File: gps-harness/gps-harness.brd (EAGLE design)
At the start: 36.3 x 40.7 mm, 7 parts

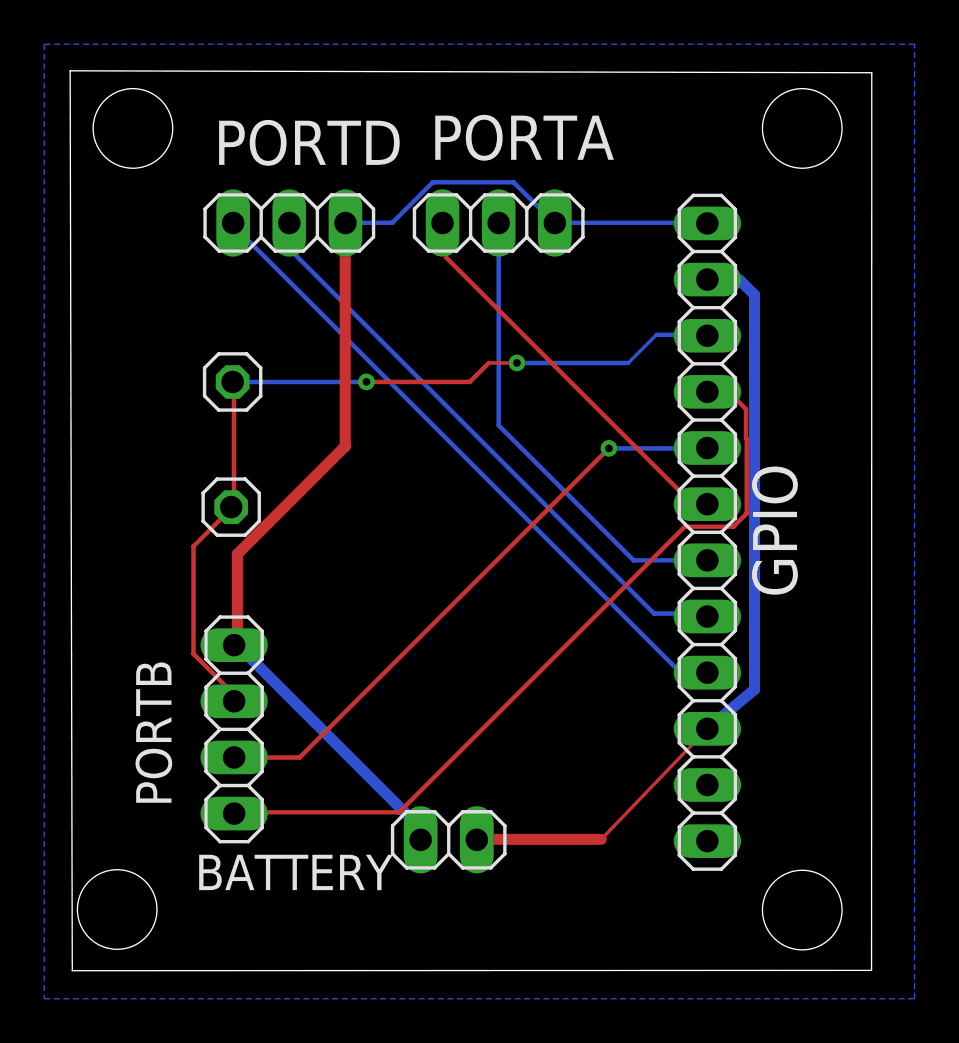
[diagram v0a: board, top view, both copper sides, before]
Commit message: Modify the place of the left bottom mounting hole; Unify the width of the wires; clear up the GND line since there's a ground plane
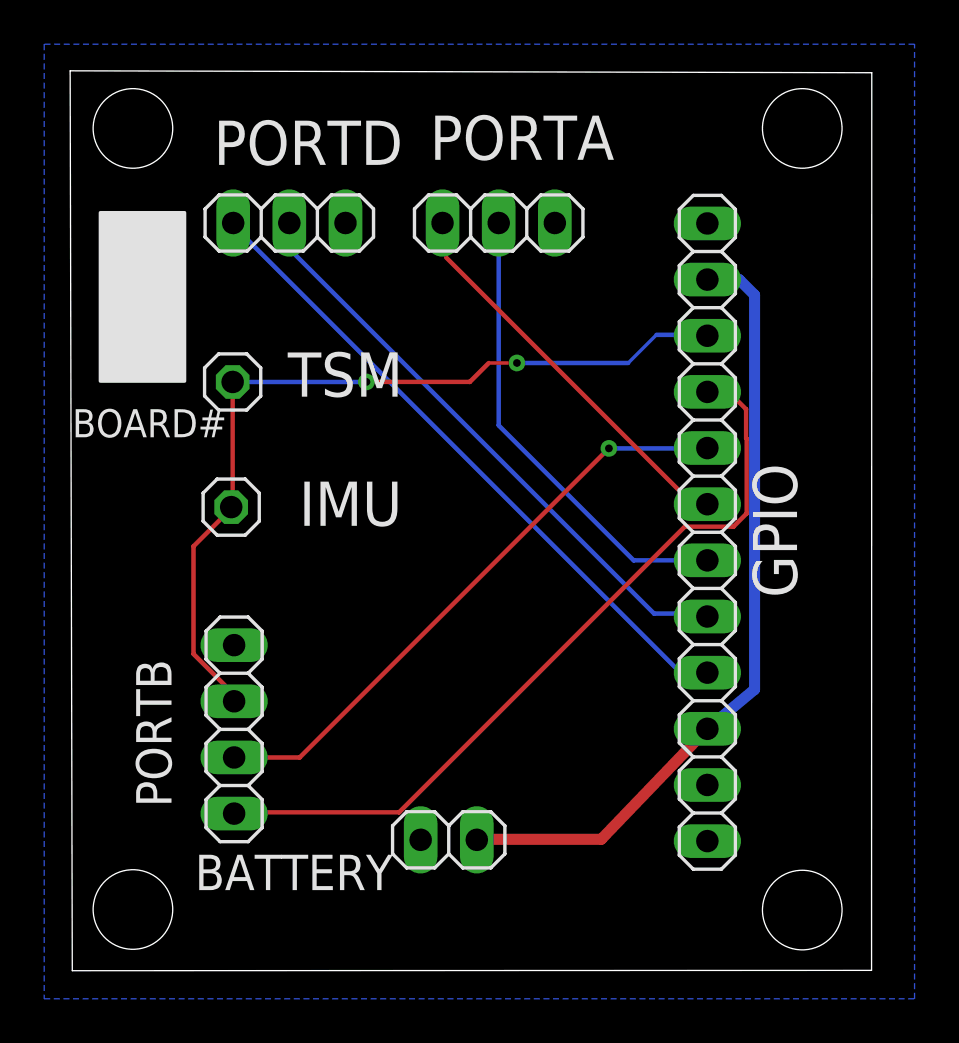
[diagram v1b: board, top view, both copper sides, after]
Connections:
- removed net NO_CONNECTION: GPIO.11, GPIO.12
- new net NC_1: GPIO.11
- new net NC_2: GPIO.12
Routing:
- net GND: track 52.0 -> 0.58 mm
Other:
- board text added: "BOARD#"
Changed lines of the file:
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@@
 <hole x="2.7432" y="38.1" drill="3.6" locked="yes"/>
 <hole x="33.02" y="2.7432" drill="3.6" locked="yes"/>
-<text x="10.256521875" y="20.124421875" size="2" layer="22">IMU</text>
-<text x="9.751059375" y="25.966421875" size="2" layer="22">TSM</text>
-<hole x="2.032" y="2.7686" drill="3.6" locked="yes"/>
+<text x="10.256521875" y="20.124421875" size="2" layer="21">IMU</text>
+<text x="9.751059375" y="25.966421875" size="2" layer="21">TSM</text>
+<hole x="2.7432" y="2.7686" drill="3.6"/>
 <hole x="33.02" y="38.1" drill="3.6" locked="yes"/>
 <text x="26.512515625" y="2.031996875" locked="yes" size="2" layer="22" rot="MR0">Autorally
@@
 v1.0
 Oct. 2019</text>
+<polygon width="0.1524" layer="21">
+<vertex x="1.27" y="34.29"/>
+<vertex x="1.27" y="26.67"/>
+<vertex x="5.08" y="26.67"/>
+<vertex x="5.08" y="34.29"/>
+</polygon>
+<text x="0" y="24.13" size="1.27" layer="21">BOARD#</text>
 </plain>
 <attributes>
@@
 <contactref element="BATTERY" pad="2"/>
 <wire x1="7.320278125" y1="14.726921875" x2="7.472675" y2="14.726921875" width="0.5" layer="16"/>
-<wire x1="16.17471875" y1="6.024878125" x2="7.472675" y2="14.726921875" width="0.5" layer="16"/>
-<wire x1="16.17471875" y1="6.024878125" x2="15.758159375" y2="5.920740625" width="0.1524" layer="16"/>
-<wire x1="14.478" y1="33.8328" x2="12.4968" y2="33.8328" width="0.2032" layer="16"/>
-<wire x1="16.3068" y1="35.6616" x2="14.478" y2="33.8328" width="0.2032" layer="16"/>
-<wire x1="19.9644" y1="35.6616" x2="16.3068" y2="35.6616" width="0.2032" layer="16"/>
-<wire x1="21.7932" y1="33.8328" x2="19.9644" y2="35.6616" width="0.2032" layer="16"/>
 <wire x1="12.4968" y1="33.8328" x2="12.3571" y2="33.822640625" width="0.1524" layer="16"/>
 <wire x1="21.7932" y1="33.8328" x2="21.8287625" y2="33.8226375" width="0.1524" layer="16"/>
-<wire x1="21.9456" y1="33.8328" x2="28.6004" y2="33.8328" width="0.2032" layer="16"/>
 <wire x1="28.6004" y1="33.8328" x2="28.7274" y2="33.802315625" width="0.1524" layer="16"/>
 <wire x1="21.9456" y1="33.8328" x2="21.8287625" y2="33.8226375" width="0.1524" layer="16"/>
-<wire x1="7.4676" y1="18.84171875" x2="7.4676" y2="14.7828" width="0.5" layer="1"/>
-<wire x1="12.3444" y1="23.71851875" x2="7.4676" y2="18.84171875" width="0.5" layer="1"/>
-<wire x1="12.3444" y1="33.6804" x2="12.3444" y2="23.71851875" width="0.5" layer="1"/>
-<wire x1="7.4676" y1="14.7828" x2="7.320278125" y2="14.726921875" width="0.1524" layer="1"/>
-<wire x1="12.3444" y1="33.6804" x2="12.3571" y2="33.822640625" width="0.1524" layer="1"/>
 <polygon width="0.1524" layer="16">
 <vertex x="-1.27" y="41.91"/>
@@
 <wire x1="23.928809375" y1="5.9436" x2="18.4404" y2="5.9436" width="0.5" layer="1"/>
 <wire x1="18.4404" y1="5.9436" x2="18.298159375" y2="5.920740625" width="0.1524" layer="1"/>
-<wire x1="23.928809375" y1="5.9436" x2="28.7274" y2="10.942315625" width="0.1524" layer="1"/>
+<wire x1="23.928809375" y1="5.9436" x2="28.7274" y2="10.942315625" width="0.5" layer="1"/>
 <wire x1="30.863540625" y1="30.563821875" x2="30.165046875" y2="31.262315625" width="0.5" layer="16"/>
 <wire x1="28.7274" y1="31.262315625" x2="30.165046875" y2="31.262315625" width="0.5" layer="16"/>
@@
 <contactref element="IMU" pad="1"/>
 <contactref element="TSY" pad="1"/>
-<wire x1="7.3152" y1="26.5176" x2="7.3152" y2="21.0312" width="0.2032" layer="1"/>
-<wire x1="7.3152" y1="21.0312" x2="7.1882" y2="20.9702375" width="0.1524" layer="1"/>
-<wire x1="7.3152" y1="26.5176" x2="7.254240625" y2="26.6319" width="0.1524" layer="1"/>
 <wire x1="7.3152" y1="12.4968" x2="7.3152" y2="12.192" width="0.1524" layer="1"/>
 <wire x1="5.4864" y1="14.3256" x2="7.3152" y2="12.4968" width="0.2032" layer="1"/>
 <wire x1="5.4864" y1="19.2024" x2="5.4864" y2="14.3256" width="0.2032" layer="1"/>
-<wire x1="7.1628" y1="20.8788" x2="5.4864" y2="19.2024" width="0.2032" layer="1"/>
 <wire x1="7.3152" y1="12.192" x2="7.320278125" y2="12.186921875" width="0.1524" layer="1"/>
-<wire x1="7.1628" y1="20.8788" x2="7.1882" y2="20.9702375" width="0.1524" layer="1"/>
 <wire x1="7.254240625" y1="26.6319" x2="13.30451875" y2="26.6319" width="0.2032" layer="16"/>
 <wire x1="13.30451875" y1="26.6319" x2="13.307059375" y2="26.634440625" width="0.1524" layer="16"/>
@@
 <wire x1="26.42108125" y1="28.762959375" x2="28.68675625" y2="28.762959375" width="0.2032" layer="16"/>
 <wire x1="28.68675625" y1="28.762959375" x2="28.7274" y2="28.722315625" width="0.1524" layer="16"/>
-</signal>
-<signal name="NO_CONNECTION">
+<wire x1="7.254240625" y1="26.6319" x2="7.254240625" y2="20.970240625" width="0.2032" layer="1"/>
+<wire x1="7.254240625" y1="20.970240625" x2="5.4864" y2="19.2024" width="0.2032" layer="1"/>
+<wire x1="7.254240625" y1="26.6319" x2="7.1882" y2="20.9702375" width="0" layer="19" extent="1-1"/>
+</signal>
+<signal name="NC_1">
 <contactref element="GPIO" pad="11"/>
+</signal>
+<signal name="NC_2">
 <contactref element="GPIO" pad="12"/>
-<wire x1="28.7274" y1="5.862315625" x2="28.7274" y2="8.402315625" width="0" layer="19" extent="1-1"/>
 </signal>
 </signals>
